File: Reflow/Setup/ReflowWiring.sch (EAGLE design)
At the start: 5 parts

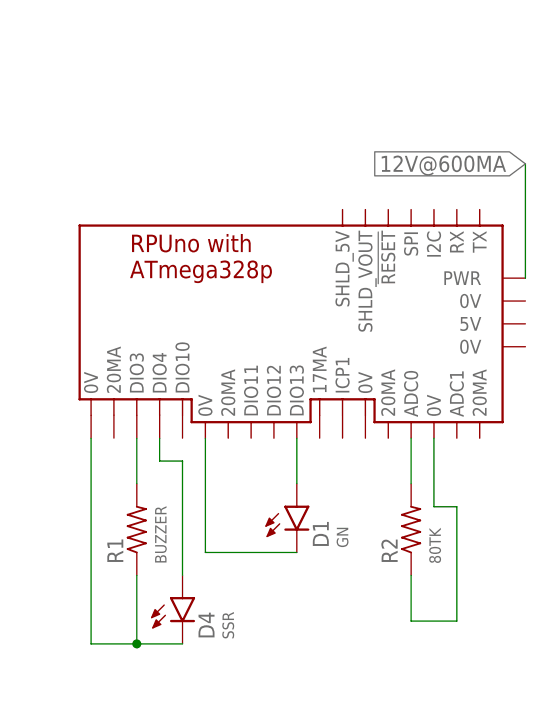
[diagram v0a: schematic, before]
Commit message: Reflow: ^9 updates and add a light sensor to start profile
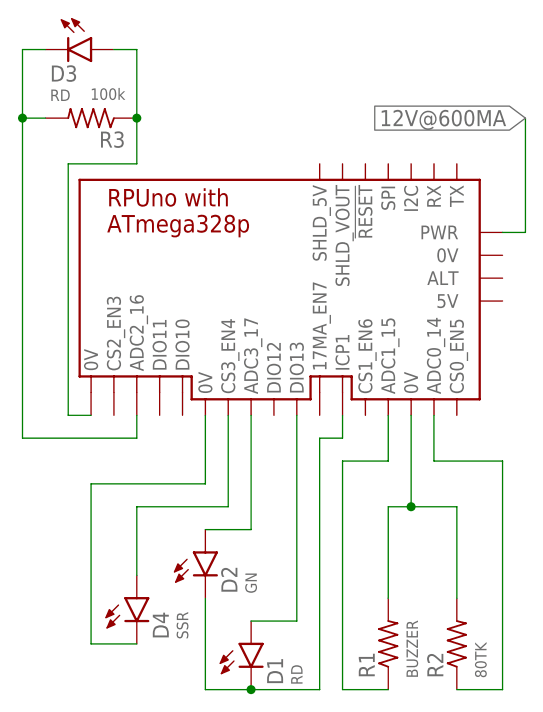
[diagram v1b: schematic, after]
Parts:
- removed BM3: (no value), Documentation:RPUNO
- added BM1: (no value), Documentation:RPUNO
- added D2: GN, D-LED:LED5MM
- added D3: RD, D-LED:LED5MM
- added R3: 100k, R-C:R0805
- D1: value GN -> RD
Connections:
- new net DIO13: BM1.DIO13, D1.A
- new net N$8: BM1.0V@5, D3.A, R3.1
- new net N$9: BM1.ADC2_16, D3.K, R3.2
- net 12V@600MA: now also BM1.PWR; no longer BM3.PWR
- net N$1: now also BM1.ADC3_17, D2.A; no longer BM3.DIO13, D1.A
- net N$2: now also BM1.ICP1, D2.K; no longer BM3.0V@6
- net N$3: now also BM1.CS3_EN4; no longer BM3.DIO4
- net N$4: now also BM1.0V@3, R1.2; no longer BM3.ADC0
- net N$5: now also BM1.0V@6; no longer BM3.0V@5, R1.1
- net N$6: now also BM1.ADC1_15, R1.1; no longer BM3.DIO3, R1.2
- net N$7: now also BM1.ADC0_14; no longer BM3.0V@3
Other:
- note added: "STATUS"
- moved on the sheet: D1, D4, R1, R2
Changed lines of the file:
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@@
 </classes>
 <parts>
-<part name="BM3" library="Documentation" deviceset="RPUNO" device=""/>
-<part name="D1" library="D-LED" deviceset="LED" device="5MM" value="GN"/>
+<part name="D1" library="D-LED" deviceset="LED" device="5MM" value="RD"/>
 <part name="D4" library="D-LED" deviceset="LED" device="5MM" value="SSR"/>
 <part name="R1" library="R-C" deviceset="R" device="0805" value="BUZZER"/>
 <part name="R2" library="R-C" deviceset="R" device="0805" value="80TK"/>
+<part name="D2" library="D-LED" deviceset="LED" device="5MM" value="GN"/>
+<part name="BM1" library="Documentation" deviceset="RPUNO" device=""/>
+<part name="D3" library="D-LED" deviceset="LED" device="5MM" value="RD"/>
+<part name="R3" library="R-C" deviceset="R" device="0805" value="100k"/>
 </parts>
 <sheets>
 <sheet>
 <plain>
-<text x="33.02" y="127" size="5.08" layer="98">REFLOW</text>
+<text x="27.94" y="134.62" size="5.08" layer="98">REFLOW</text>
+<text x="39.878" y="75.946" size="1.27" layer="98" rot="R90">STATUS</text>
+<text x="37.338" y="86.106" size="1.27" layer="98" rot="R90">REFLOW</text>
 </plain>
 <instances>
-<instance part="BM3" gate="G$1" x="45.72" y="109.22"/>
-<instance part="D1" gate="G$1" x="40.64" y="86.36"/>
-<instance part="D4" gate="G$1" x="27.94" y="76.2"/>
-<instance part="R1" gate="G$1" x="22.86" y="83.82" rot="R90"/>
-<instance part="R2" gate="G$1" x="53.34" y="83.82" rot="R90"/>
+<instance part="D1" gate="G$1" x="35.56" y="71.12"/>
+<instance part="D4" gate="G$1" x="22.86" y="76.2"/>
+<instance part="R1" gate="G$1" x="50.8" y="71.12" rot="R90"/>
+<instance part="R2" gate="G$1" x="58.42" y="71.12" rot="R90"/>
+<instance part="D2" gate="G$1" x="30.48" y="81.28"/>
+<instance part="BM1" gate="G$1" x="43.18" y="111.76"/>
+<instance part="D3" gate="G$1" x="17.78" y="137.16" rot="R270"/>
+<instance part="R3" gate="G$1" x="17.78" y="129.54" rot="R180"/>
 </instances>
 <busses>
@@
 <net name="12V@600MA" class="0">
 <segment>
-<pinref part="BM3" gate="G$1" pin="PWR"/>
-<wire x1="66.04" y1="111.76" x2="66.04" y2="124.46" width="0.1524" layer="91"/>
-<label x="66.04" y="124.46" size="1.778" layer="91" rot="R180" xref="yes"/>
+<wire x1="66.04" y1="116.84" x2="66.04" y2="129.54" width="0.1524" layer="91"/>
+<label x="66.04" y="129.54" size="1.778" layer="91" rot="R180" xref="yes"/>
+<pinref part="BM1" gate="G$1" pin="PWR"/>
+<wire x1="66.04" y1="116.84" x2="63.5" y2="116.84" width="0.1524" layer="91"/>
 </segment>
 </net>
-<net name="N$1" class="0">
+<net name="DIO13" class="0">
 <segment>
 <pinref part="D1" gate="G$1" pin="A"/>
-<pinref part="BM3" gate="G$1" pin="DIO13"/>
-<wire x1="40.64" y1="93.98" x2="40.64" y2="88.9" width="0.1524" layer="91"/>
+<wire x1="40.64" y1="96.52" x2="40.64" y2="73.66" width="0.1524" layer="91"/>
+<wire x1="40.64" y1="73.66" x2="35.56" y2="73.66" width="0.1524" layer="91"/>
+<pinref part="BM1" gate="G$1" pin="DIO13"/>
 </segment>
 </net>
@@
 <segment>
 <pinref part="D1" gate="G$1" pin="K"/>
-<pinref part="BM3" gate="G$1" pin="0V@6"/>
-<wire x1="40.64" y1="81.28" x2="30.48" y2="81.28" width="0.1524" layer="91"/>
-<wire x1="30.48" y1="81.28" x2="30.48" y2="93.98" width="0.1524" layer="91"/>
+<wire x1="35.56" y1="66.04" x2="30.48" y2="66.04" width="0.1524" layer="91"/>
+<wire x1="30.48" y1="66.04" x2="30.48" y2="76.2" width="0.1524" layer="91"/>
+<pinref part="D2" gate="G$1" pin="K"/>
+<wire x1="35.56" y1="66.04" x2="43.18" y2="66.04" width="0.1524" layer="91"/>
+<junction x="35.56" y="66.04"/>
+<wire x1="43.18" y1="66.04" x2="43.18" y2="93.98" width="0.1524" layer="91"/>
+<wire x1="43.18" y1="93.98" x2="45.72" y2="93.98" width="0.1524" layer="91"/>
+<wire x1="45.72" y1="93.98" x2="45.72" y2="96.52" width="0.1524" layer="91"/>
+<pinref part="BM1" gate="G$1" pin="ICP1"/>
 </segment>
 </net>
@@
 <segment>
 <pinref part="D4" gate="G$1" pin="A"/>
-<wire x1="27.94" y1="91.44" x2="27.94" y2="78.74" width="0.1524" layer="91"/>
-<pinref part="BM3" gate="G$1" pin="DIO4"/>
-<wire x1="25.4" y1="91.44" x2="27.94" y2="91.44" width="0.1524" layer="91"/>
-<wire x1="25.4" y1="93.98" x2="25.4" y2="91.44" width="0.1524" layer="91"/>
+<wire x1="22.86" y1="86.36" x2="22.86" y2="78.74" width="0.1524" layer="91"/>
+<wire x1="22.86" y1="86.36" x2="33.02" y2="86.36" width="0.1524" layer="91"/>
+<pinref part="BM1" gate="G$1" pin="CS3_EN4"/>
+<wire x1="33.02" y1="86.36" x2="33.02" y2="96.52" width="0.1524" layer="91"/>
 </segment>
 </net>
@@
 <segment>
 <pinref part="D4" gate="G$1" pin="K"/>
-<pinref part="BM3" gate="G$1" pin="0V@5"/>
-<wire x1="27.94" y1="71.12" x2="22.86" y2="71.12" width="0.1524" layer="91"/>
 <wire x1="22.86" y1="71.12" x2="17.78" y2="71.12" width="0.1524" layer="91"/>
-<wire x1="17.78" y1="71.12" x2="17.78" y2="93.98" width="0.1524" layer="91"/>
-<pinref part="R1" gate="G$1" pin="1"/>
-<wire x1="22.86" y1="78.74" x2="22.86" y2="71.12" width="0.1524" layer="91"/>
-<junction x="22.86" y="71.12"/>
-</segment>
-</net>
-<net name="N$6" class="0">
-<segment>
-<pinref part="R1" gate="G$1" pin="2"/>
-<pinref part="BM3" gate="G$1" pin="DIO3"/>
-<wire x1="22.86" y1="88.9" x2="22.86" y2="93.98" width="0.1524" layer="91"/>
+<wire x1="17.78" y1="71.12" x2="17.78" y2="88.9" width="0.1524" layer="91"/>
+<pinref part="BM1" gate="G$1" pin="0V@6"/>
+<wire x1="17.78" y1="88.9" x2="30.48" y2="88.9" width="0.1524" layer="91"/>
+<wire x1="30.48" y1="88.9" x2="30.48" y2="96.52" width="0.1524" layer="91"/>
 </segment>
 </net>
 <net name="N$4" class="0">
 <segment>
-<pinref part="BM3" gate="G$1" pin="ADC0"/>
 <pinref part="R2" gate="G$1" pin="2"/>
-<wire x1="53.34" y1="93.98" x2="53.34" y2="88.9" width="0.1524" layer="91"/>
+<pinref part="R1" gate="G$1" pin="2"/>
+<wire x1="58.42" y1="76.2" x2="58.42" y2="86.36" width="0.1524" layer="91"/>
+<wire x1="58.42" y1="86.36" x2="53.34" y2="86.36" width="0.1524" layer="91"/>
+<wire x1="53.34" y1="86.36" x2="50.8" y2="86.36" width="0.1524" layer="91"/>
+<wire x1="50.8" y1="86.36" x2="50.8" y2="76.2" width="0.1524" layer="91"/>
+<pinref part="BM1" gate="G$1" pin="0V@3"/>
+<wire x1="53.34" y1="96.52" x2="53.34" y2="86.36" width="0.1524" layer="91"/>
+<junction x="53.34" y="86.36"/>
 </segment>
 </net>
@@
 <segment>
 <pinref part="R2" gate="G$1" pin="1"/>
-<wire x1="53.34" y1="78.74" x2="53.34" y2="73.66" width="0.1524" layer="91"/>
-<wire x1="53.34" y1="73.66" x2="58.42" y2="73.66" width="0.1524" layer="91"/>
-<wire x1="58.42" y1="73.66" x2="58.42" y2="86.36" width="0.1524" layer="91"/>
-<pinref part="BM3" gate="G$1" pin="0V@3"/>
-<wire x1="58.42" y1="86.36" x2="55.88" y2="86.36" width="0.1524" layer="91"/>
-<wire x1="55.88" y1="86.36" x2="55.88" y2="93.98" width="0.1524" layer="91"/>
+<wire x1="58.42" y1="66.04" x2="63.5" y2="66.04" width="0.1524" layer="91"/>
+<wire x1="63.5" y1="66.04" x2="63.5" y2="91.44" width="0.1524" layer="91"/>
+<wire x1="63.5" y1="91.44" x2="55.88" y2="91.44" width="0.1524" layer="91"/>
+<pinref part="BM1" gate="G$1" pin="ADC0_14"/>
+<wire x1="55.88" y1="91.44" x2="55.88" y2="96.52" width="0.1524" layer="91"/>
 </segment>
 </net>
+<net name="N$1" class="0">
+<segment>
+<pinref part="D2" gate="G$1" pin="A"/>
+<wire x1="30.48" y1="83.82" x2="35.56" y2="83.82" width="0.1524" layer="91"/>
+<wire x1="35.56" y1="83.82" x2="35.56" y2="96.52" width="0.1524" layer="91"/>
+<pinref part="BM1" gate="G$1" pin="ADC3_17"/>
+</segment>
+</net>
+<net name="N$6" class="0">
+<segment>
+<pinref part="R1" gate="G$1" pin="1"/>
+<wire x1="50.8" y1="66.04" x2="45.72" y2="66.04" width="0.1524" layer="91"/>
+<pinref part="BM1" gate="G$1" pin="ADC1_15"/>
+<wire x1="45.72" y1="66.04" x2="45.72" y2="91.44" width="0.1524" layer="91"/>
+<wire x1="45.72" y1="91.44" x2="50.8" y2="91.44" width="0.1524" layer="91"/>
+<wire x1="50.8" y1="91.44" x2="50.8" y2="96.52" width="0.1524" layer="91"/>
+</segment>
+</net>
+<net name="N$8" class="0">
+<segment>
+<pinref part="D3" gate="G$1" pin="A"/>
+<wire x1="20.32" y1="137.16" x2="22.86" y2="137.16" width="0.1524" layer="91"/>
+<wire x1="22.86" y1="137.16" x2="22.86" y2="129.54" width="0.1524" layer="91"/>
+<wire x1="22.86" y1="129.54" x2="22.86" y2="124.46" width="0.1524" layer="91"/>
+<wire x1="22.86" y1="124.46" x2="15.24" y2="124.46" width="0.1524" layer="91"/>
+<wire x1="15.24" y1="124.46" x2="15.24" y2="96.52" width="0.1524" layer="91"/>
+<pinref part="BM1" gate="G$1" pin="0V@5"/>
+<wire x1="15.24" y1="96.52" x2="17.78" y2="96.52" width="0.1524" layer="91"/>
+<pinref part="R3" gate="G$1" pin="1"/>
+<junction x="22.86" y="129.54"/>
+</segment>
+</net>
+<net name="N$9" class="0">
+<segment>
+<pinref part="D3" gate="G$1" pin="K"/>
+<wire x1="12.7" y1="137.16" x2="10.16" y2="137.16" width="0.1524" layer="91"/>
+<wire x1="10.16" y1="137.16" x2="10.16" y2="129.54" width="0.1524" layer="91"/>
+<pinref part="BM1" gate="G$1" pin="ADC2_16"/>
+<wire x1="10.16" y1="129.54" x2="10.16" y2="93.98" width="0.1524" layer="91"/>
+<wire x1="10.16" y1="93.98" x2="22.86" y2="93.98" width="0.1524" layer="91"/>
+<wire x1="22.86" y1="93.98" x2="22.86" y2="96.52" width="0.1524" layer="91"/>
+<pinref part="R3" gate="G$1" pin="2"/>
+<wire x1="12.7" y1="129.54" x2="10.16" y2="129.54" width="0.1524" layer="91"/>
+<junction x="10.16" y="129.54"/>
+</segment>
+</net>
